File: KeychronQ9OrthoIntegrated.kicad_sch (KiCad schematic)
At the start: 167 parts, among them J1 Conn_01x07, J2 USB_C_Receptacle_USB2.0_16P, J3 Conn_01x05, U1 XC6206PxxxMR, U2 SRV05-4, U3 RP2040, U4 W25Q128JVS, Y1 Crystal_GND24

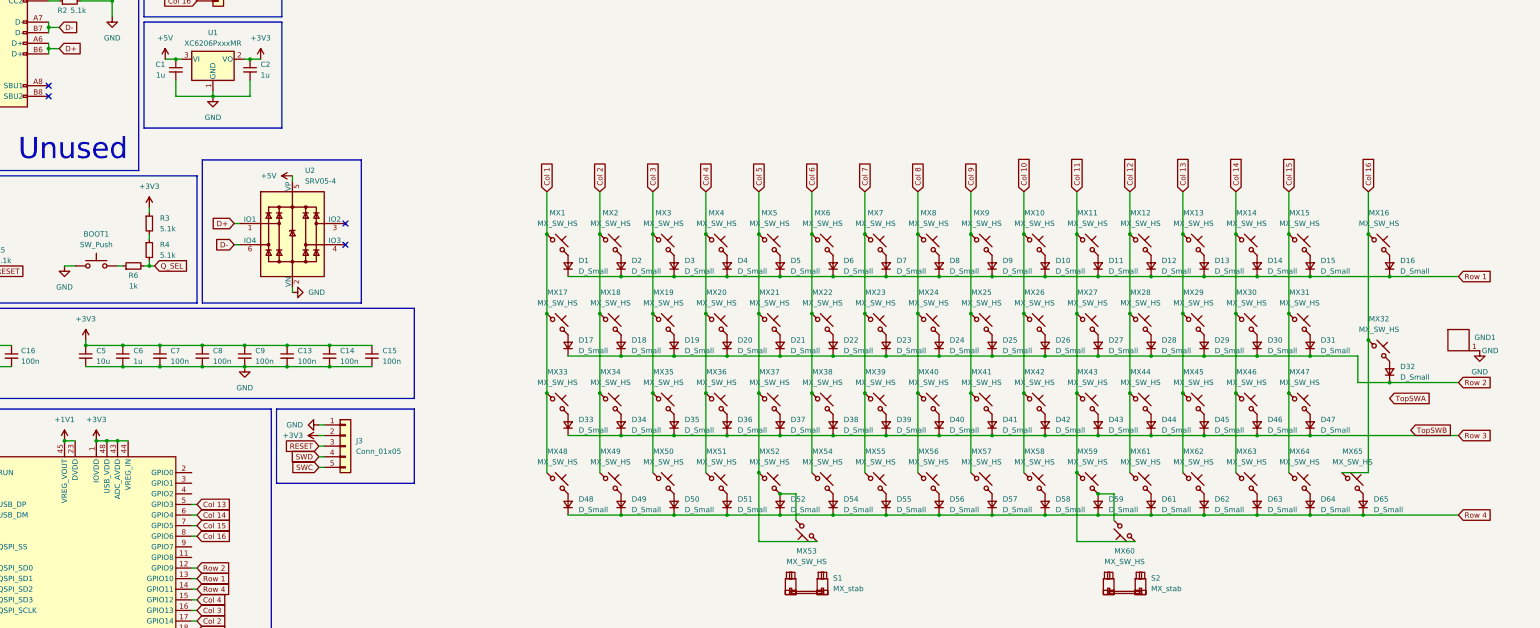
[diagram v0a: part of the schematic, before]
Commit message: add encoders, ground fill, production files
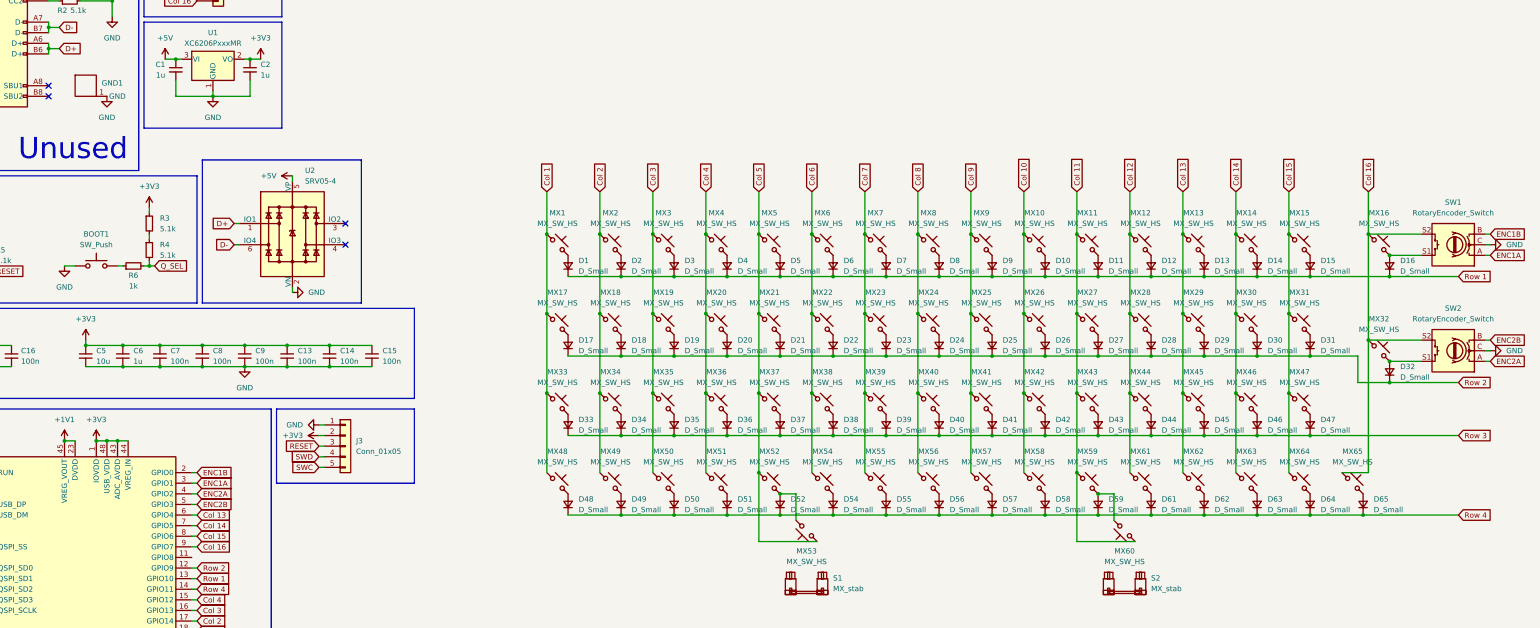
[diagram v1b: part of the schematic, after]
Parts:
- added SW1, SW2: RotaryEncoder_Switch, PCM_marbastlib-various:ROT_Alps_EC11E-Switch, symbol Device:RotaryEncoder_Switch
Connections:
- net Col 13: now also U3.6 (GPIO4); no longer U3.5 (GPIO3)
- net Col 14: now also U3.7 (GPIO5); no longer U3.6 (GPIO4)
- net Col 15: now also U3.8 (GPIO6); no longer U3.7 (GPIO5)
- net Col 16: now also U3.9 (GPIO7), SW1.S2, SW2.S2; no longer U3.8 (GPIO6)
- net GND: now also SW1.C, SW2.C
- net at D16.2 (A), MX16.2: now also SW1.S1
- net at D32.2 (A), MX32.2: now also SW2.S1
- net ENC1B: now reaches U3.2 (GPIO0)
- net ENC1B: now also SW1.B
- net ENC1A: now reaches U3.3 (GPIO1)
- net ENC1A: now also SW1.A
- net ENC2A: now reaches U3.4 (GPIO2)
- net ENC2A: now also SW2.A
- new net ENC2B: SW2.B, U3.5 (GPIO3)
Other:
- moved on the sheet: GND1

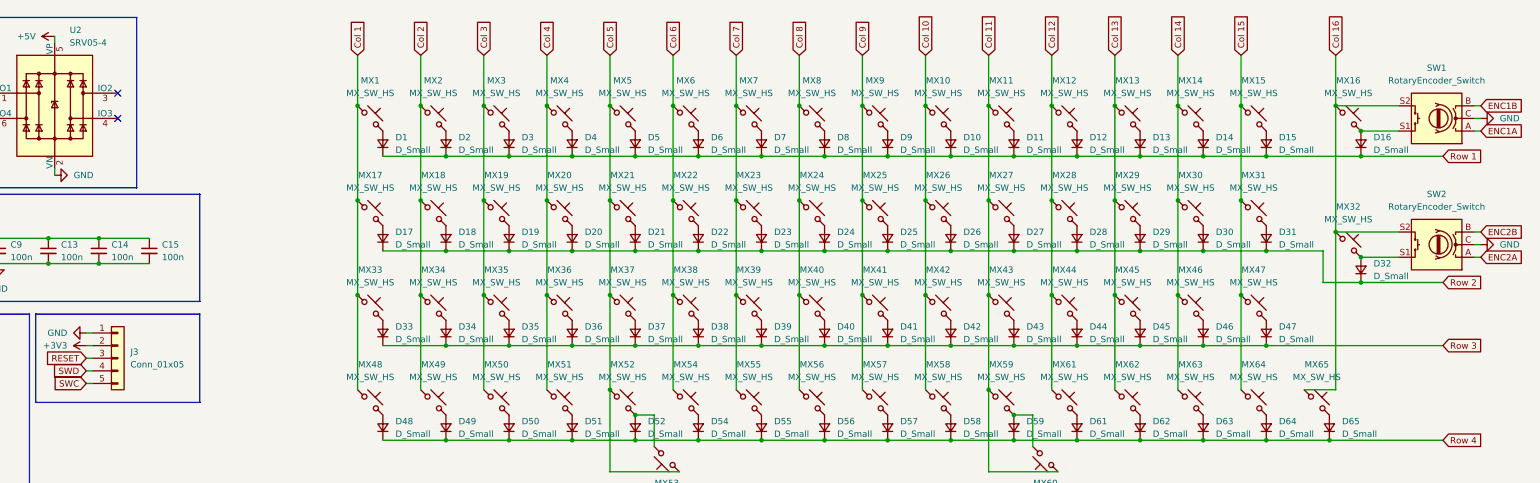
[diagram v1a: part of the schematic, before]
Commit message: fix silkscreen/solder mask conflicts
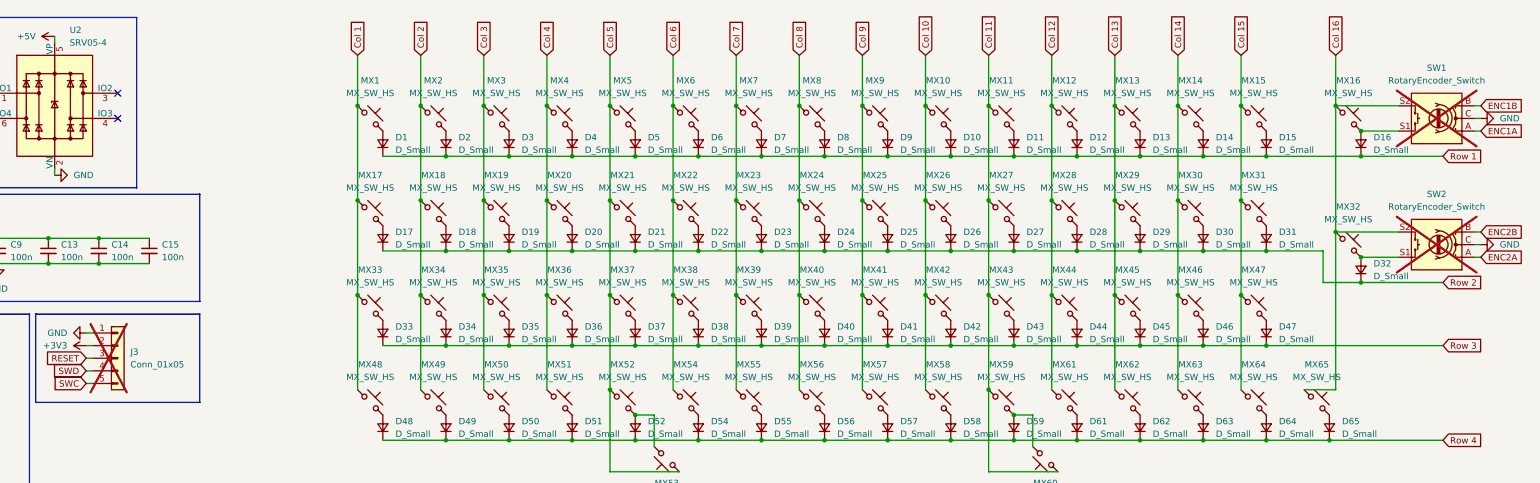
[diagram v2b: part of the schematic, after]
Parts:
- D1, D10, D11, D12, D13, D14, D15, D16, D17, D18, D19, D2, D20, D21, D22, D23, D24, D25, D26, D27, D28, D29, D3, D30, D31, D32, D33, D34, D35, D36, D37, D38, D39, D4, D40, D41, D42, D43, D44, D45, D46, D47, D48, D49, D5, D50, D51, D52, D54, D55, D56, D57, D58, D59, D6, D61, D62, D63, D64, D65, D7, D8, D9: footprint Diode_SMD:D_SOD-123 -> xomm:D_SOD-123_xomm
- J3, SW1, SW2: now not fitted; now left out of the parts list
- MX16, MX32, MX52, MX53, MX54, MX59, MX60, MX61: footprint PCM_marbastlib-mx:SW_MX_HS_CPG151101S11_1u -> PCM_marbastlib-mx:SW_MX_HS_S_CPG151101S11_1u

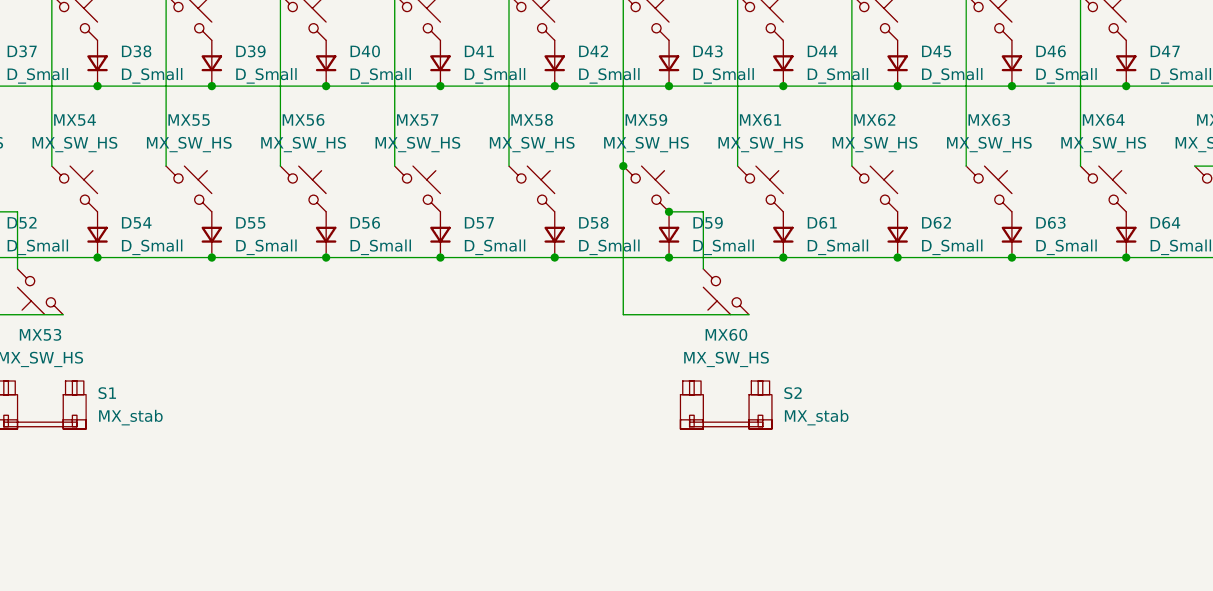
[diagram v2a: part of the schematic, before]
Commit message: add back right side numpad layout
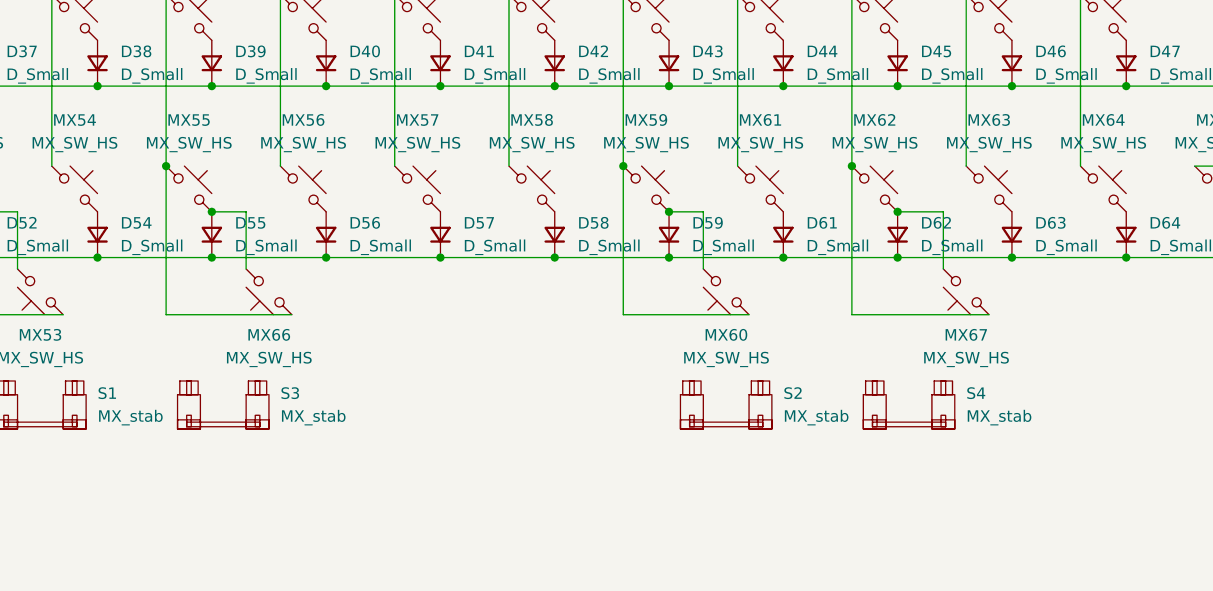
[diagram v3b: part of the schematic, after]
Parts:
- added MX66, MX67: MX_SW_HS, PCM_marbastlib-mx:SW_MX_HS_S_CPG151101S11_1u, symbol PCM_marbastlib-mx:MX_SW_HS_CPG151101S11
- added S3, S4: MX_stab, PCM_marbastlib-mx:STAB_MX_P_2u, symbol PCM_marbastlib-mx:MX_stab
- MX1, MX2, MX3, MX55, MX56, MX62, MX63: footprint PCM_marbastlib-mx:SW_MX_HS_CPG151101S11_1u -> PCM_marbastlib-mx:SW_MX_HS_S_CPG151101S11_1u
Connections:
- net Col 13: now also MX67.1
- net Col 7: now also MX66.1
- net at D62.2 (A), MX62.2: now also MX67.2
- net at D55.2 (A), MX55.2: now also MX66.2

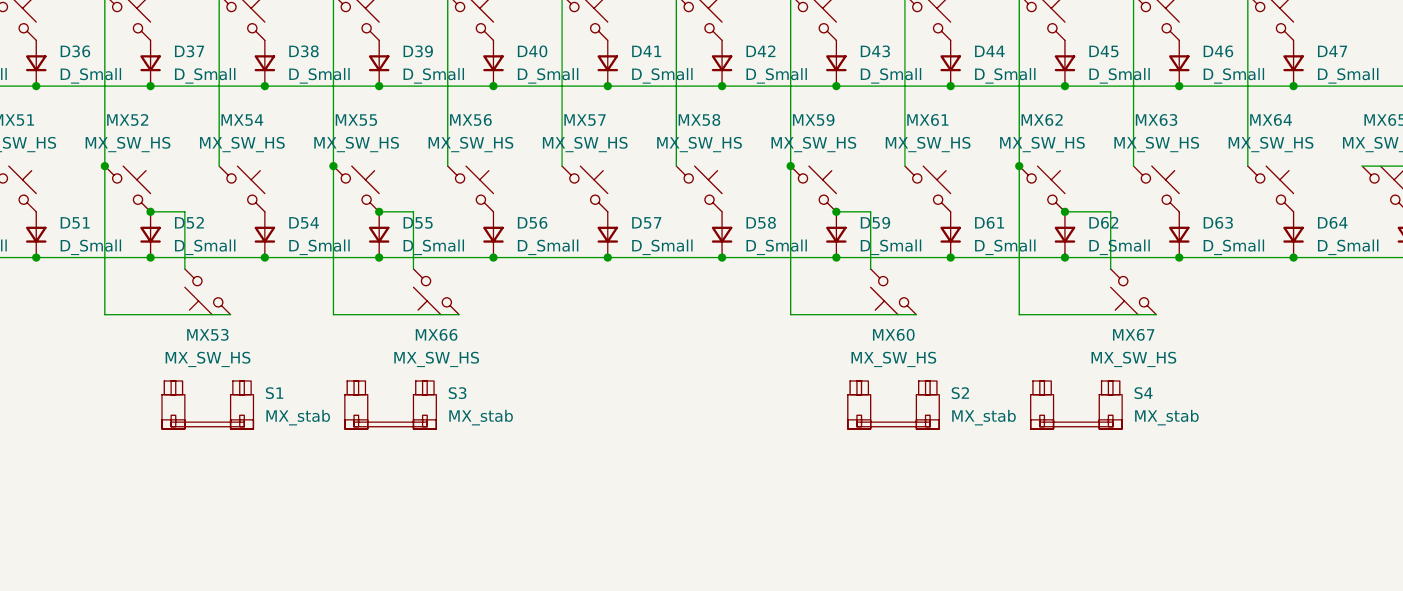
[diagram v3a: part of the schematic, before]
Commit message: add spacebar for 3u center cluster
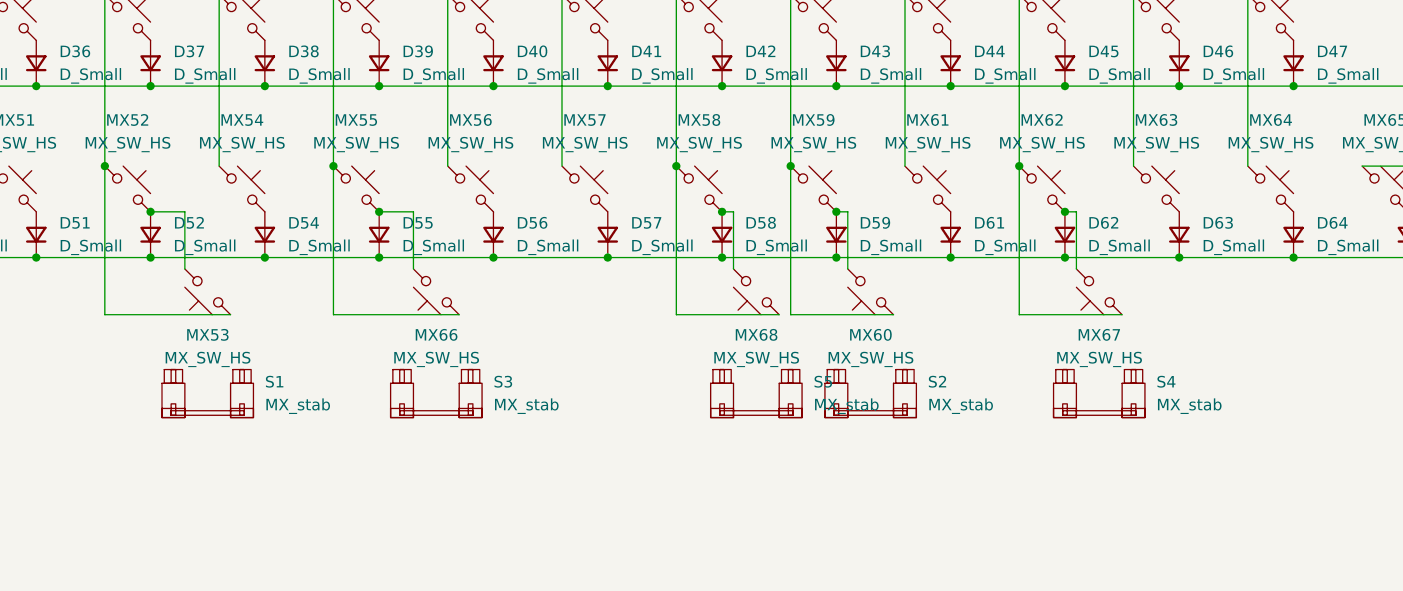
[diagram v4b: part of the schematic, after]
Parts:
- added MX68: MX_SW_HS, PCM_marbastlib-mx:SW_MX_HS_S_CPG151101S11_1u, symbol PCM_marbastlib-mx:MX_SW_HS_CPG151101S11
- added S5: MX_stab, PCM_marbastlib-mx:STAB_MX_P_2u, symbol PCM_marbastlib-mx:MX_stab
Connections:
- net Col 10: now also MX68.1
- net at D58.2 (A), MX58.2: now also MX68.2
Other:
- moved on the sheet: MX60, MX67, S1, S2, S3, S4

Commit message: add ortho plate subproject
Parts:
- MX58: footprint PCM_marbastlib-mx:SW_MX_HS_CPG151101S11_1u -> PCM_marbastlib-mx:SW_MX_HS_S_CPG151101S11_1u
- S1, S2, S3, S4, S5: now left out of the parts list
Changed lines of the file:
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@@
 		(unit 1)
 		(exclude_from_sim no)
-		(in_bom yes)
+		(in_bom no)
 		(on_board yes)
 		(dnp no)
@@
 		(unit 1)
 		(exclude_from_sim no)
-		(in_bom yes)
+		(in_bom no)
 		(on_board yes)
 		(dnp no)
@@
 		(unit 1)
 		(exclude_from_sim no)
-		(in_bom yes)
+		(in_bom no)
 		(on_board yes)
 		(dnp no)
@@
 			)
 		)
-		(property "Footprint" "PCM_marbastlib-mx:SW_MX_HS_CPG151101S11_1u"
+		(property "Footprint" "PCM_marbastlib-mx:SW_MX_HS_S_CPG151101S11_1u"
 			(at 281.94 148.59 0)
 			(effects
@@
 		(unit 1)
 		(exclude_from_sim no)
-		(in_bom yes)
+		(in_bom no)
 		(on_board yes)
 		(dnp no)
@@
 		(unit 1)
 		(exclude_from_sim no)
-		(in_bom yes)
+		(in_bom no)
 		(on_board yes)
 		(dnp no)
